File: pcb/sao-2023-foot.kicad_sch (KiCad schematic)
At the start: 3 parts, among them J1 Conn_02x03_Odd_Even

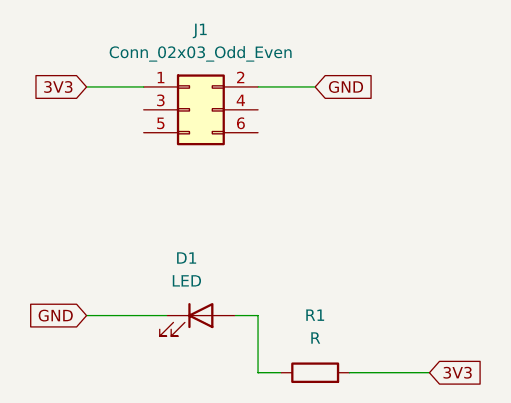
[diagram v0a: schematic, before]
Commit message: Corrected SAO Connector (#4)
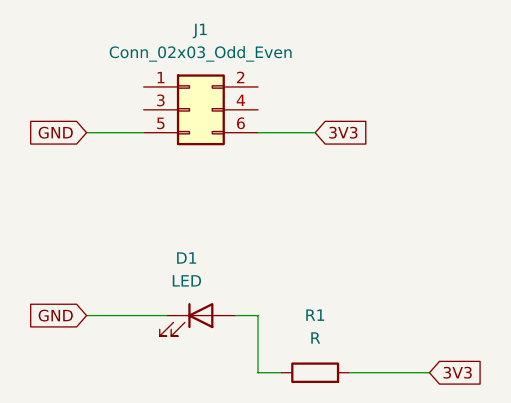
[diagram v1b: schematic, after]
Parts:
- J1: footprint Connector_PinSocket_2.54mm:PinSocket_2x03_P2.54mm_Vertical_SMD -> Connector_PinHeader_2.54mm:PinHeader_2x03_P2.54mm_Vertical_SMD
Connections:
- net 3V3: now also J1.6 (Pin_6); no longer J1.1 (Pin_1)
- net GND: now also J1.5 (Pin_5); no longer J1.2 (Pin_2)
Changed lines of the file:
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@@
-    (stroke (width 0) (type default))
-  )
-  (wire (pts (xy 88.9 63.5) (xy 95.25 63.5))
     (stroke (width 0) (type default))
   )
   (wire (pts (xy 107.95 95.25) (xy 110.49 95.25))
-    (stroke (width 0) (type default))
-  )
-  (wire (pts (xy 107.95 63.5) (xy 114.3 63.5))
     (stroke (width 0) (type default))
   )
@@
     (stroke (width 0) (type default))
   )
-  (global_label "3V3" (shape input) (at 88.9 63.5 180) (fields_autoplaced)
-    (effects (font (size 1.27 1.27)) (justify right))
-    (property "Intersheetrefs" "${INTERSHEET_REFS}" (at 82.4866 63.5 0)
-      (effects (font (size 1.27 1.27)) (justify right) hide)
+  (wire (pts (xy 88.9 68.58) (xy 95.25 68.58))
+    (stroke (width 0) (type default))
+  )
+  (wire (pts (xy 107.95 68.58) (xy 114.3 68.58))
+    (stroke (width 0) (type default))
+  )
+  (global_label "3V3" (shape input) (at 114.3 68.58 0) (fields_autoplaced)
+    (effects (font (size 1.27 1.27)) (justify left))
+    (property "Intersheetrefs" "${INTERSHEET_REFS}" (at 120.7134 68.58 0)
+      (effects (font (size 1.27 1.27)) (justify left) hide)
     )
   )
@@
     )
   )
-  (global_label "GND" (shape input) (at 114.3 63.5 0) (fields_autoplaced)
-    (effects (font (size 1.27 1.27)) (justify left))
-    (property "Intersheetrefs" "${INTERSHEET_REFS}" (at 121.0763 63.5 0)
-      (effects (font (size 1.27 1.27)) (justify left) hide)
+  (global_label "GND" (shape input) (at 88.9 68.58 180) (fields_autoplaced)
+    (effects (font (size 1.27 1.27)) (justify right))
+    (property "Intersheetrefs" "${INTERSHEET_REFS}" (at 82.1237 68.58 0)
+      (effects (font (size 1.27 1.27)) (justify right) hide)
     )
   )
@@
       (effects (font (size 1.27 1.27)))
     )
-    (property "Footprint" "Connector_PinSocket_2.54mm:PinSocket_2x03_P2.54mm_Vertical_SMD" (at 100.33 66.04 0)
+    (property "Footprint" "Connector_PinHeader_2.54mm:PinHeader_2x03_P2.54mm_Vertical_SMD" (at 100.33 66.04 0)
       (effects (font (size 1.27 1.27)) hide)
     )
